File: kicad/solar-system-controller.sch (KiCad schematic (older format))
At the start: 20 parts, among them J1 Raspberry_Pi_2_3, J2 Line_In, U1 MCP3008, U2 500 Gain, U3 1000 Gain

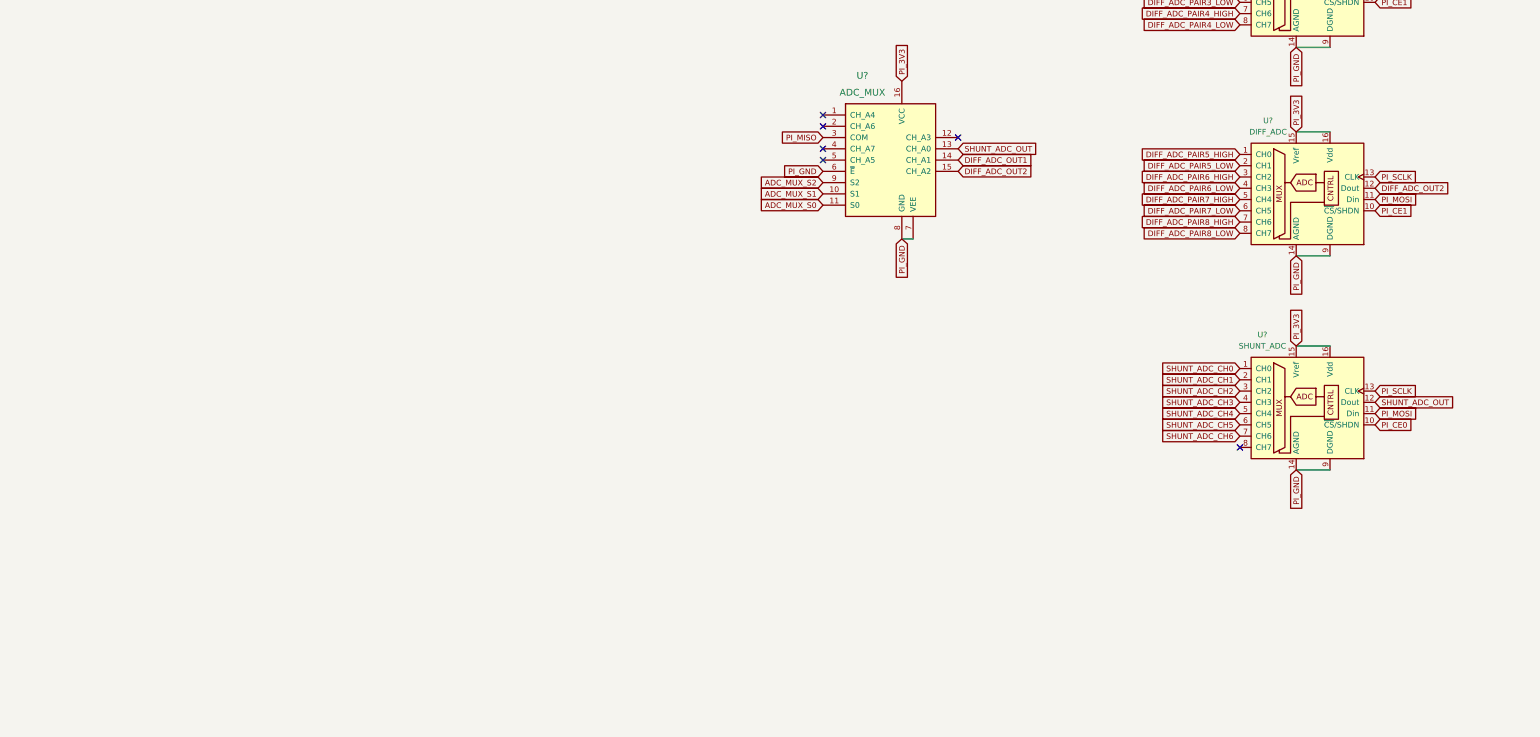
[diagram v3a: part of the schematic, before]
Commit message: Finished initial pass of the AC voltage monitor using a transformer.
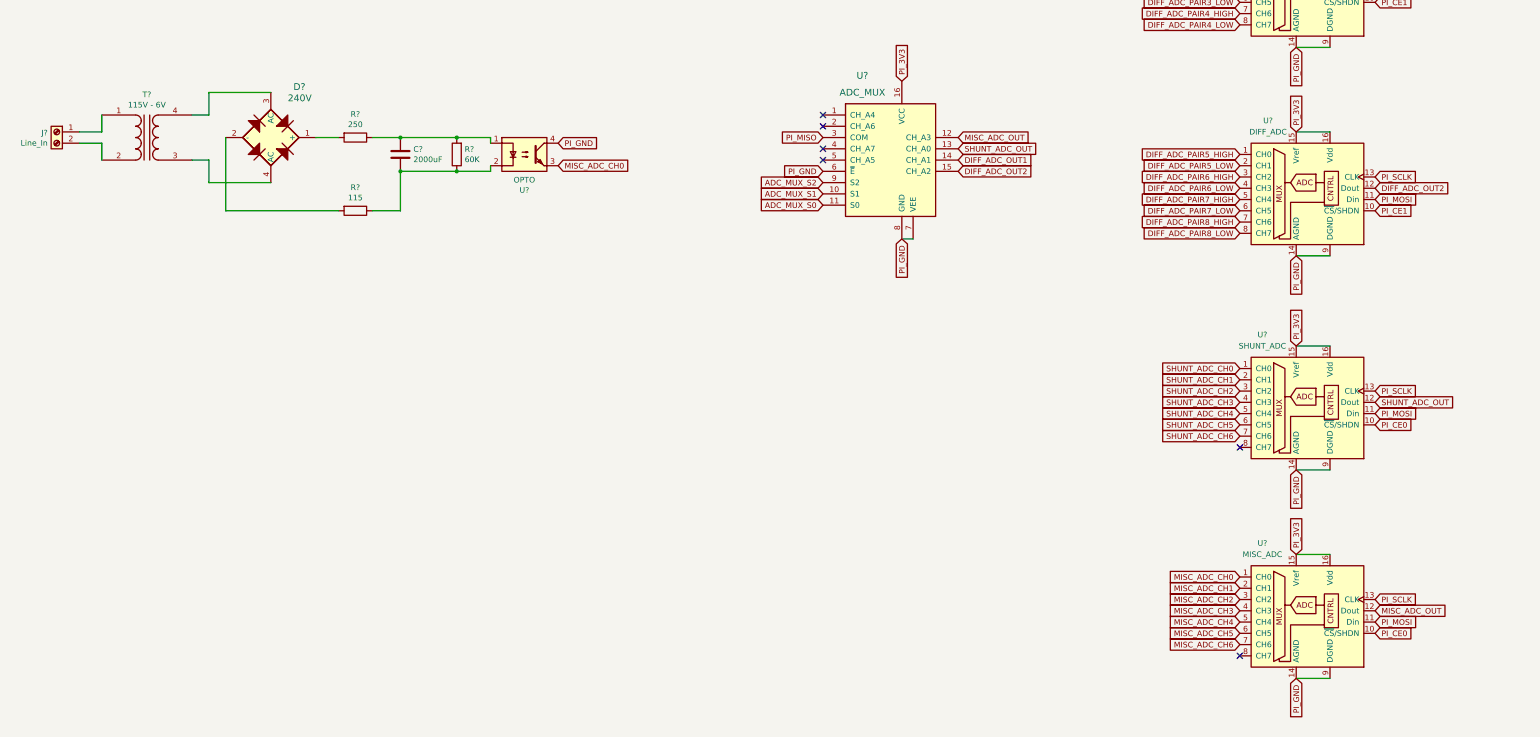
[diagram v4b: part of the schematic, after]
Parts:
- added C?: 2000uF, symbol Device:C
- added D?: 240V, digikey-footprints:DIP-4_W7.62mm, symbol dk_Diodes-Bridge-Rectifiers:DF04M
- added J?: Line_In, digikey-footprints:Term_Block_1x2_P5.08MM, symbol Connector:Screw_Terminal_01x02
- added R?: 60K, symbol Device:R
- added R?: 115, symbol Device:R
- added R?: 250, symbol Device:R
- added T?: 115V - 6V, symbol Device:Transformer_1P_1S
- added U?: MISC_ADC, Package_DIP:DIP-16_W7.62mm, symbol Analog_ADC:MCP3008
- added U?: OPTO, Package_DIP:DIP-4_W7.62mm, symbol Isolator:LTV-817
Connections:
- net PI_3V3: now also U?.15 (Vref), U?.16 (Vdd)
- net PI_CE0: now also U?.10 (~CS~/SHDN)
- net PI_GND: now also U?.14 (AGND), U?.4, U?.9 (DGND)
- net PI_MOSI: now also U?.11 (Din)
- net PI_SCLK: now also U?.13 (CLK)
- net MISC_ADC_OUT: now reaches U?.12 (CH_A3)
- net MISC_ADC_OUT: now also U?.12 (Dout)
- new net: C?.1, R?.1, R?.2, U?.1
- new net: C?.2, R?.1, R?.1, U?.2
- new net: J?.1 (Pin_1), T?.1 (AA)
- new net: J?.2 (Pin_2), T?.2 (AB)
- new net: D?.1 (+), R?.2
- new net: D?.2 (-), R?.2
- new net: D?.3 (AC), T?.4 (SB)
- new net: D?.4 (AC), T?.3 (SA)
- new net MISC_ADC_CH0: U?.1 (CH0), U?.3
- new net MISC_ADC_CH1: U?.2 (CH1)
- new net MISC_ADC_CH2: U?.3 (CH2)
- new net MISC_ADC_CH3: U?.4 (CH3)
- new net MISC_ADC_CH4: U?.5 (CH4)
- new net MISC_ADC_CH5: U?.6 (CH5)
- new net MISC_ADC_CH6: U?.7 (CH6)
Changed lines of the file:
@@
 Wire Wire Line
 	8950 10250 9050 10250
-NoConn ~ 9450 9350
 NoConn ~ 8250 9150
 NoConn ~ 8250 9250
@@
 Text GLabel 3900 2750 2    50   Input ~ 0
 ADC_MUX_S0
+$Comp
+L Analog_ADC:MCP3008 U?
+U 1 1 61134328
+P 12550 13550
+F 0 "U?" H 12150 14150 50  0000 C CNN
+F 1 "MISC_ADC" H 12150 14050 50  0000 C CNN
+F 2 "Package_DIP:DIP-16_W7.62mm" H 12650 13650 50  0001 C CNN
+F 3 "http://ww1.microchip.com/downloads/en/DeviceDoc/21295d.pdf" H 12650 13650 50  0001 C CNN
+F 4 "https://www.digikey.com/en/products/detail/microchip-technology/MCP3008-I-P/319422" H 12550 13550 50  0001 C CNN "Part"
+	1    12550 13550
+	1    0    0    -1
+$EndComp
+Text GLabel 12450 14150 3    50   Input ~ 0
+PI_GND
+Wire Wire Line
+	12450 14150 12750 14150
+Text GLabel 12450 13050 1    50   Input ~ 0
+PI_3V3
+Wire Wire Line
+	12450 13050 12750 13050
+Text GLabel 11950 13250 0    50   Input ~ 0
+MISC_ADC_CH0
+Text GLabel 11950 13350 0    50   Input ~ 0
+MISC_ADC_CH1
+Text GLabel 11950 13450 0    50   Input ~ 0
+MISC_ADC_CH2
+Text GLabel 11950 13550 0    50   Input ~ 0
+MISC_ADC_CH3
+Text GLabel 11950 13650 0    50   Input ~ 0
+MISC_ADC_CH4
+Text GLabel 11950 13750 0    50   Input ~ 0
+MISC_ADC_CH5
+Text GLabel 11950 13850 0    50   Input ~ 0
+MISC_ADC_CH6
+Text GLabel 13150 13450 2    50   Input ~ 0
+PI_SCLK
+Text GLabel 13150 13550 2    50   Input ~ 0
+MISC_ADC_OUT
+Text GLabel 13150 13650 2    50   Input ~ 0
+PI_MOSI
+Text GLabel 13150 13750 2    50   Input ~ 0
+PI_CE0
+NoConn ~ 11950 13950
+Text GLabel 9450 9350 2    50   Input ~ 0
+MISC_ADC_OUT
+$Comp
+L Device:C C?
+U 1 1 6116A3B9
+P 4500 9500
+F 0 "C?" H 4615 9546 50  0000 L CNN
+F 1 "2000uF" H 4615 9455 50  0000 L CNN
+F 2 "" H 4538 9350 50  0001 C CNN
+F 3 "~" H 4500 9500 50  0001 C CNN
+	1    4500 9500
+	1    0    0    -1
+$EndComp
+$Comp
+L Connector:Screw_Terminal_01x02 J?
+U 1 1 6116A3C0
+P 1450 9300
+F 0 "J?" H 1530 9292 50  0000 L CNN
+F 1 "Line_In" H 1530 9201 50  0000 L CNN
+F 2 "digikey-footprints:Term_Block_1x2_P5.08MM" H 1450 9300 50  0001 C CNN
+F 3 "https://www.we-online.de/katalog/datasheet/691137710002.pdf" H 1450 9300 50  0001 C CNN
+F 4 "https://www.digikey.com/en/products/detail/w%C3%BCrth-elektronik/691137710002/6644051" H 1450 9300 50  0001 C CNN "Part"
+	1    1450 9300
+	-1   0    0    -1
+$EndComp
+Connection ~ 4500 9350
+$Comp
+L Device:R R?
+U 1 1 6116A3CD
+P 5000 9500
+F 0 "R?" H 4930 9454 50  0000 R CNN
+F 1 "60K" H 4930 9545 50  0000 R CNN
+F 2 "" V 4930 9500 50  0001 C CNN
+F 3 "~" H 5000 9500 50  0001 C CNN
+	1    5000 9500
+	-1   0    0    1
+$EndComp
+Wire Wire Line
+	4500 9350 5000 9350
+Wire Wire Line
+	4500 9650 5000 9650
+Wire Wire Line
+	4500 10000 4500 9650
+Connection ~ 4500 9650
+$Comp
+L Device:R R?
+U 1 1 6116A3E9
+P 4100 10000
+F 0 "R?" V 3893 10000 50  0000 C CNN
+F 1 "115" V 3984 10000 50  0000 C CNN
+F 2 "" V 4030 10000 50  0001 C CNN
+F 3 "~" H 4100 10000 50  0001 C CNN
+	1    4100 10000
+	0    1    1    0
+$EndComp
+$Comp
+L Device:R R?
+U 1 1 6116A3F9
+P 4100 9350
+F 0 "R?" V 3893 9350 50  0000 C CNN
+F 1 "250" V 3984 9350 50  0000 C CNN
+F 2 "" V 4030 9350 50  0001 C CNN
+F 3 "~" H 4100 9350 50  0001 C CNN
+	1    4100 9350
+	0    1    1    0
+$EndComp
+Wire Wire Line
+	4250 9350 4500 9350
+Wire Wire Line
+	4250 10000 4500 10000
+Text GLabel 5900 9600 2    50   Input ~ 0
+MISC_ADC_CH0
+Text GLabel 5900 9400 2    50   Input ~ 0
+PI_GND
+$Comp
+L Isolator:LTV-817 U?
+U 1 1 6116A404
+P 5600 9500
+F 0 "U?" H 5600 9183 50  0000 C CNN
+F 1 "OPTO" H 5600 9274 50  0000 C CNN
+F 2 "Package_DIP:DIP-4_W7.62mm" H 5400 9300 50  0001 L CIN
+F 3 "http://www.us.liteon.com/downloads/LTV-817-827-847.PDF" H 5600 9400 50  0001 L CNN
+F 4 "https://www.digikey.com/en/products/detail/lite-on-inc/LTV-817/385836" H 5600 9500 50  0001 C CNN "Part"
+	1    5600 9500
+	1    0    0    -1
+$EndComp
+Wire Wire Line
+	5000 9350 5300 9350
+Wire Wire Line
+	5300 9350 5300 9400
+Connection ~ 5000 9350
+Wire Wire Line
+	5000 9650 5300 9650
+Wire Wire Line
+	5300 9650 5300 9600
+Connection ~ 5000 9650
+$Comp
+L Device:Transformer_1P_1S T?
+U 1 1 6116FC74
+P 2250 9350
+F 0 "T?" H 2250 9731 50  0000 C CNN
+F 1 "115V - 6V" H 2250 9640 50  0000 C CNN
+F 2 "" H 2250 9350 50  0001 C CNN
+F 3 "https://www.zettlermagnetics.com/pdfs/EI30_06.pdf" H 2250 9350 50  0001 C CNN
+F 4 "https://www.digikey.com/en/products/detail/zettler-magnetics/BV301S06006-ZU/12093244" H 2250 9350 50  0001 C CNN "Part"
+	1    2250 9350
+	1    0    0    -1
+$EndComp
+Wire Wire Line
+	1650 9300 1850 9300
+Wire Wire Line
+	1850 9300 1850 9150
+Wire Wire Line
+	1650 9400 1850 9400
+Wire Wire Line
+	1850 9400 1850 9550
+Wire Wire Line
+	2650 9150 2800 9150
+Wire Wire Line
+	2650 9550 2800 9550
+$Comp
+L dk_Diodes-Bridge-Rectifiers:DF04M D?
+U 1 1 6116A3DF
+P 3350 9350
+F 0 "D?" H 3550 9800 60  0000 L CNN
+F 1 "240V" H 3500 9700 60  0000 L CNN
+F 2 "digikey-footprints:DIP-4_W7.62mm" H 3550 9550 60  0001 L CNN
+F 3 "https://www.onsemi.com/pub/Collateral/DF10M-D.pdf" H 3550 9650 60  0001 L CNN
+F 4 "DF04M-ND" H 3550 9750 60  0001 L CNN "Digi-Key_PN"
+F 5 "DF04M" H 3550 9850 60  0001 L CNN "MPN"
+F 6 "Discrete Semiconductor Products" H 3550 9950 60  0001 L CNN "Category"
+F 7 "Diodes - Bridge Rectifiers" H 3550 10050 60  0001 L CNN "Family"
+F 8 "https://www.onsemi.com/pub/Collateral/DF10M-D.pdf" H 3550 10150 60  0001 L CNN "DK_Datasheet_Link"
+F 9 "/product-detail/en/on-semiconductor/DF04M/DF04M-ND/965265" H 3550 10250 60  0001 L CNN "DK_Detail_Page"
+F 10 "BRIDGE RECT 1P 400V 1.5A 4DIP" H 3550 10350 60  0001 L CNN "Description"
+F 11 "ON Semiconductor" H 3550 10450 60  0001 L CNN "Manufacturer"
+F 12 "Active" H 3550 10550 60  0001 L CNN "Status"
+F 13 "https://www.digikey.com/en/products/detail/on-semiconductor/DF04M/965265" H 3350 9350 50  0001 C CNN "Part"
+	1    3350 9350
+	1    0    0    -1
+$EndComp
+Wire Wire Line
+	2800 9150 2800 8950
+Wire Wire Line
+	2800 8950 3350 8950
+Wire Wire Line
+	2800 9550 2800 9750
+Wire Wire Line
+	2800 9750 3350 9750
+Wire Wire Line
+	3750 9350 3950 9350
+Wire Wire Line
+	2950 9350 2950 10000
+Wire Wire Line
+	2950 10000 3950 10000
 $EndSCHEMATC
